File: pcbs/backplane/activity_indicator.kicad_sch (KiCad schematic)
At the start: 7 parts

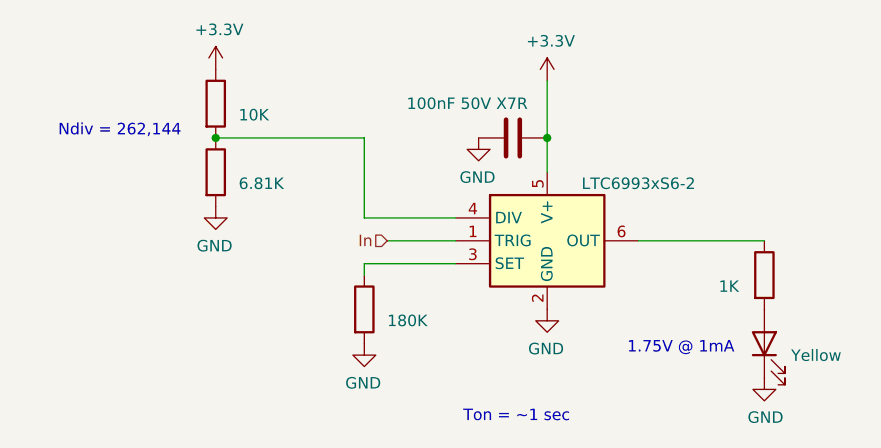
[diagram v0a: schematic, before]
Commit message: Schematic file fix, misc. PCB
Fixed issue with KiCAD's automatic V5→V6 migration (corrected in 6.0.11) that caused problems with component references in multi-channel schematic sheets
Finished migration in amp ctrl PCB, inc. re-assigning "exclude from BOM" attributes to testpoints, solder jumpers
Added mounting hole to amp ctrl PCB for addl support to Ethernet jacks, power connector through stiffener
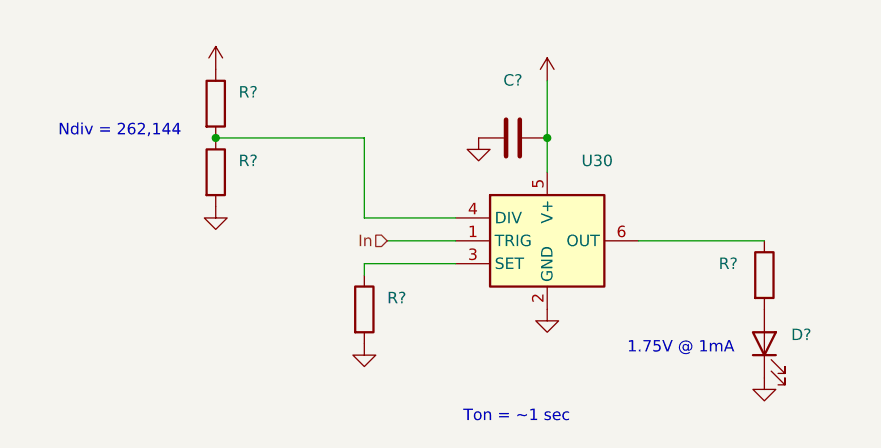
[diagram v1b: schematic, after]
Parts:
- C?: renamed from ?; value 100nF 50V X7R -> (none); footprint Capacitor_SMD:C_0603_1608Metric -> (none)
- D?: renamed from ?; value Yellow -> (none); footprint LED_SMD:LED_0805_2012Metric -> (none)
- R?: renamed from ?; value 10K -> (none); footprint Resistor_SMD:R_0805_2012Metric -> (none)
- R?: renamed from ?; value 6.81K -> (none); footprint Resistor_SMD:R_0805_2012Metric -> (none)
- R?: renamed from ?; value 1K -> (none); footprint Resistor_SMD:R_0805_2012Metric -> (none)
- R?: renamed from ?; value 180K -> (none); footprint Resistor_SMD:R_0805_2012Metric -> (none)
- U30: renamed from ?; value LTC6993xS6-2 -> (none); footprint Martinos_std:TSOT-23-6 -> (none)

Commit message: Amp ctrl: lengthened ADC & DAC reset delay to ~50 ms (#14) Backplane: added clock multiplier for 10 Mhz scanner clock (fixes #21) Backplane: reduced R5 from 10 to 1 ohm, to avoid excessive voltage drop (#20) Backplane: replaced 15V regulator with efficient voltage limiter (#20) Backplane: changed all mounting holes to signal ground Backplane: replaced +2.5V regulator with a higher-current model to support FPGA I/O bank current draw Updated to KiCAD 8
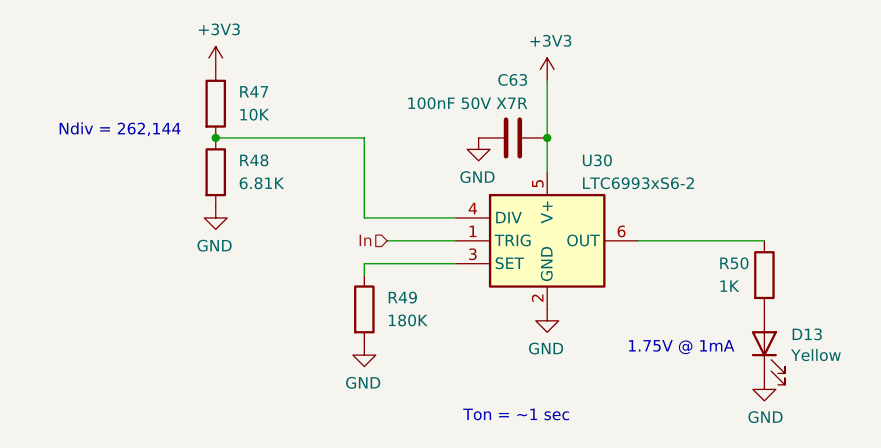
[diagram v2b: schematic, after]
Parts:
- C63: renamed from C?; value (none) -> 100nF 50V X7R; footprint (none) -> Capacitor_SMD:C_0603_1608Metric
- D13: renamed from D?; value (none) -> Yellow; footprint (none) -> LED_SMD:LED_0805_2012Metric
- R47: renamed from R?; value (none) -> 10K; footprint (none) -> Resistor_SMD:R_0805_2012Metric
- R48: renamed from R?; value (none) -> 6.81K; footprint (none) -> Resistor_SMD:R_0805_2012Metric
- R49: renamed from R?; value (none) -> 180K; footprint (none) -> Resistor_SMD:R_0805_2012Metric
- R50: renamed from R?; value (none) -> 1K; footprint (none) -> Resistor_SMD:R_0805_2012Metric
- U30: value (none) -> LTC6993xS6-2; footprint (none) -> Martinos_std:TSOT-23-6

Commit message: Corrected power-up behavior
Backplane: Inverted polarity of Shutdown_Force (now Power_Enable_FPGA), to keep amps powered off until software starts: fixes #23
Backplane: Routed Shutdown_Force to unused pin 3 on RJ45 jack B to amp boards: fixes #23
Backplane: Added pull-up and pull-down resistors to fanout buffer inputs, to keep SCK & ~LDAC signals in proper state during power-on: fixes #23
Amp control: Added transistor to reset DAC & ADC from pin 3 of RJ45 jack B
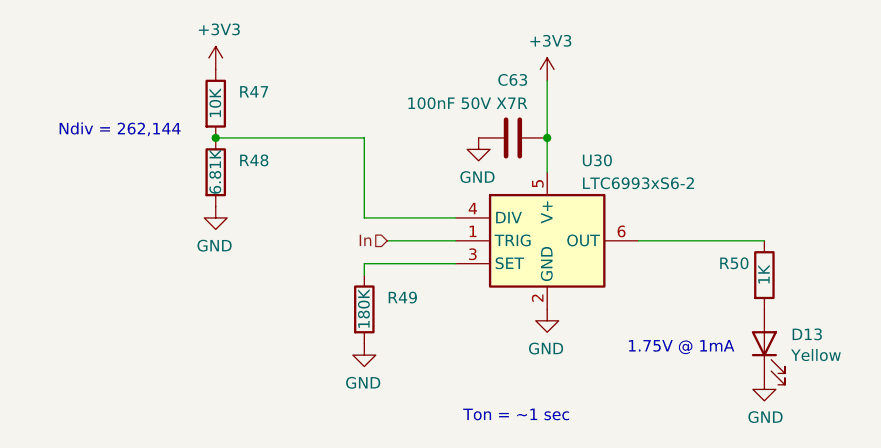
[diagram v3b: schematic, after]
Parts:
- U30: footprint Martinos_std:TSOT-23-6 -> Don_std:TSOT-23-6
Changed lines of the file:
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@@
 		(shape input)
 		(at 123.19 91.44 180)
-		(fields_autoplaced yes)
 		(effects
 			(font
@@
 			)
 		)
-		(property "Footprint" "Martinos_std:TSOT-23-6"
+		(property "Footprint" "Don_std:TSOT-23-6"
 			(at 140.97 101.6 0)
 			(effects
@@
 		)
 		(property "Value" "10K"
-			(at 106.68 77.47 0)
-			(effects
-				(font
-					(size 1.27 1.27)
-				)
-				(justify left)
+			(at 104.14 76.2 90)
+			(effects
+				(font
+					(size 1.27 1.27)
+				)
 			)
 		)
@@
 		)
 		(property "Value" "6.81K"
-			(at 106.68 85.09 0)
-			(effects
-				(font
-					(size 1.27 1.27)
-				)
-				(justify left)
+			(at 104.14 83.82 90)
+			(effects
+				(font
+					(size 1.27 1.27)
+				)
 			)
 		)
@@
 		)
 		(property "Value" "1K"
-			(at 160.02 96.52 0)
-			(effects
-				(font
-					(size 1.27 1.27)
-				)
-				(justify left)
+			(at 165.1 95.25 90)
+			(effects
+				(font
+					(size 1.27 1.27)
+				)
 			)
 		)
@@
 		)
 		(property "Value" "180K"
-			(at 123.19 100.33 0)
-			(effects
-				(font
-					(size 1.27 1.27)
-				)
-				(justify left)
-			)
-		)
+			(at 120.65 99.06 90)
+			(effects
+				(font
+					(size 1.27 1.27)
+				)
+			)
+		)

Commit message: Moved all project-specific symbols & footprints into new "shim" libraries Updated projects to reference the new "shim" library
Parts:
- U30: footprint Don_std:TSOT-23-6 -> Package_TO_SOT_SMD:TSOT-23-6
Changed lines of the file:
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@@
 			)
 		)
-		(property "Footprint" "Don_std:TSOT-23-6"
+		(property "Footprint" "Package_TO_SOT_SMD:TSOT-23-6"
 			(at 140.97 101.6 0)
 			(effects
